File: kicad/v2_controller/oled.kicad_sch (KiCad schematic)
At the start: 9 parts, among them U2 SSD1306_I2C

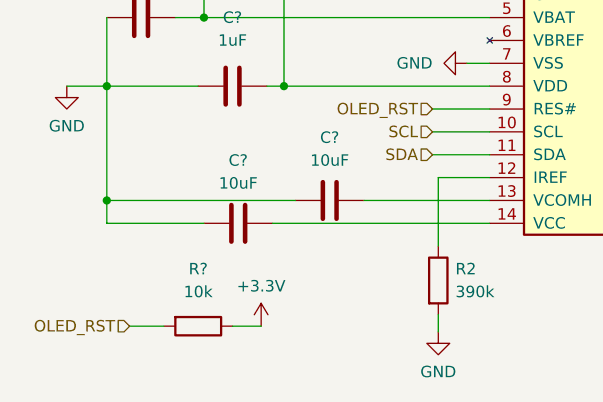
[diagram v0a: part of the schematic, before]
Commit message: [kicad] finish initial component placement
This will probably need to be tweaked further once I begin routing,
but is a start for now.
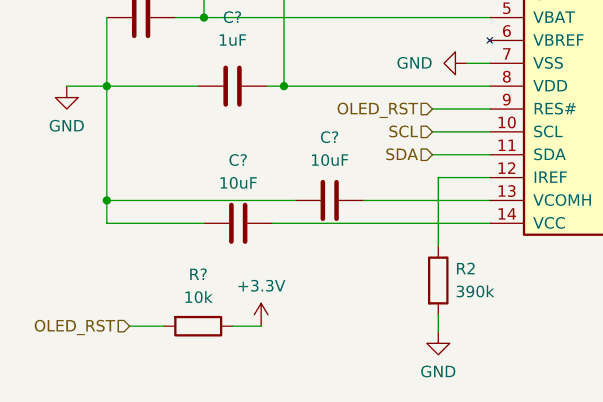
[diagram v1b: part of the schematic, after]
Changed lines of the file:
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@@
   (symbol (lib_id "Device:R") (at 52.705 85.725 270) (unit 1)
     (in_bom yes) (on_board yes) (dnp no) (fields_autoplaced)
-    (property "Reference" "R?" (at 52.705 79.375 90)
-      (effects (font (size 1.27 1.27)))
-    )
-    (property "Value" "10k" (at 52.705 81.915 90)
+    (property "Reference" "R?" (at 52.705 80.01 90)
+      (effects (font (size 1.27 1.27)))
+    )
+    (property "Value" "10k" (at 52.705 82.55 90)
       (effects (font (size 1.27 1.27)))
     )
@@
         )
         (path "/102c646f-89e8-474a-be69-05b634400329/e9d106a9-5000-4667-94d4-a7bfa9242bd9"
-          (reference "R2") (unit 1)
+          (reference "R17") (unit 1)
         )
       )
@@
         )
         (path "/102c646f-89e8-474a-be69-05b634400329/e9d106a9-5000-4667-94d4-a7bfa9242bd9"
-          (reference "R3") (unit 1)
-        )
-      )
+          (reference "R18") (unit 1)
+        )
+      )

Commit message: [kicad] switch OLED to mount on the back, folding the FPC connector
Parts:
- U2: footprint mantyl:SSD1306_OLED-0.91-128x32_Back_Mount -> mantyl:SSD1306_OLED-0.91-128x32_Folded
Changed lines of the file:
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@@
       (effects (font (size 1.27 1.27)) (justify left))
     )
-    (property "Footprint" "mantyl:SSD1306_OLED-0.91-128x32_Back_Mount" (at 90.17 56.515 0)
+    (property "Footprint" "mantyl:SSD1306_OLED-0.91-128x32_Folded" (at 90.17 56.515 0)
       (effects (font (size 1.27 1.27)) hide)
     )

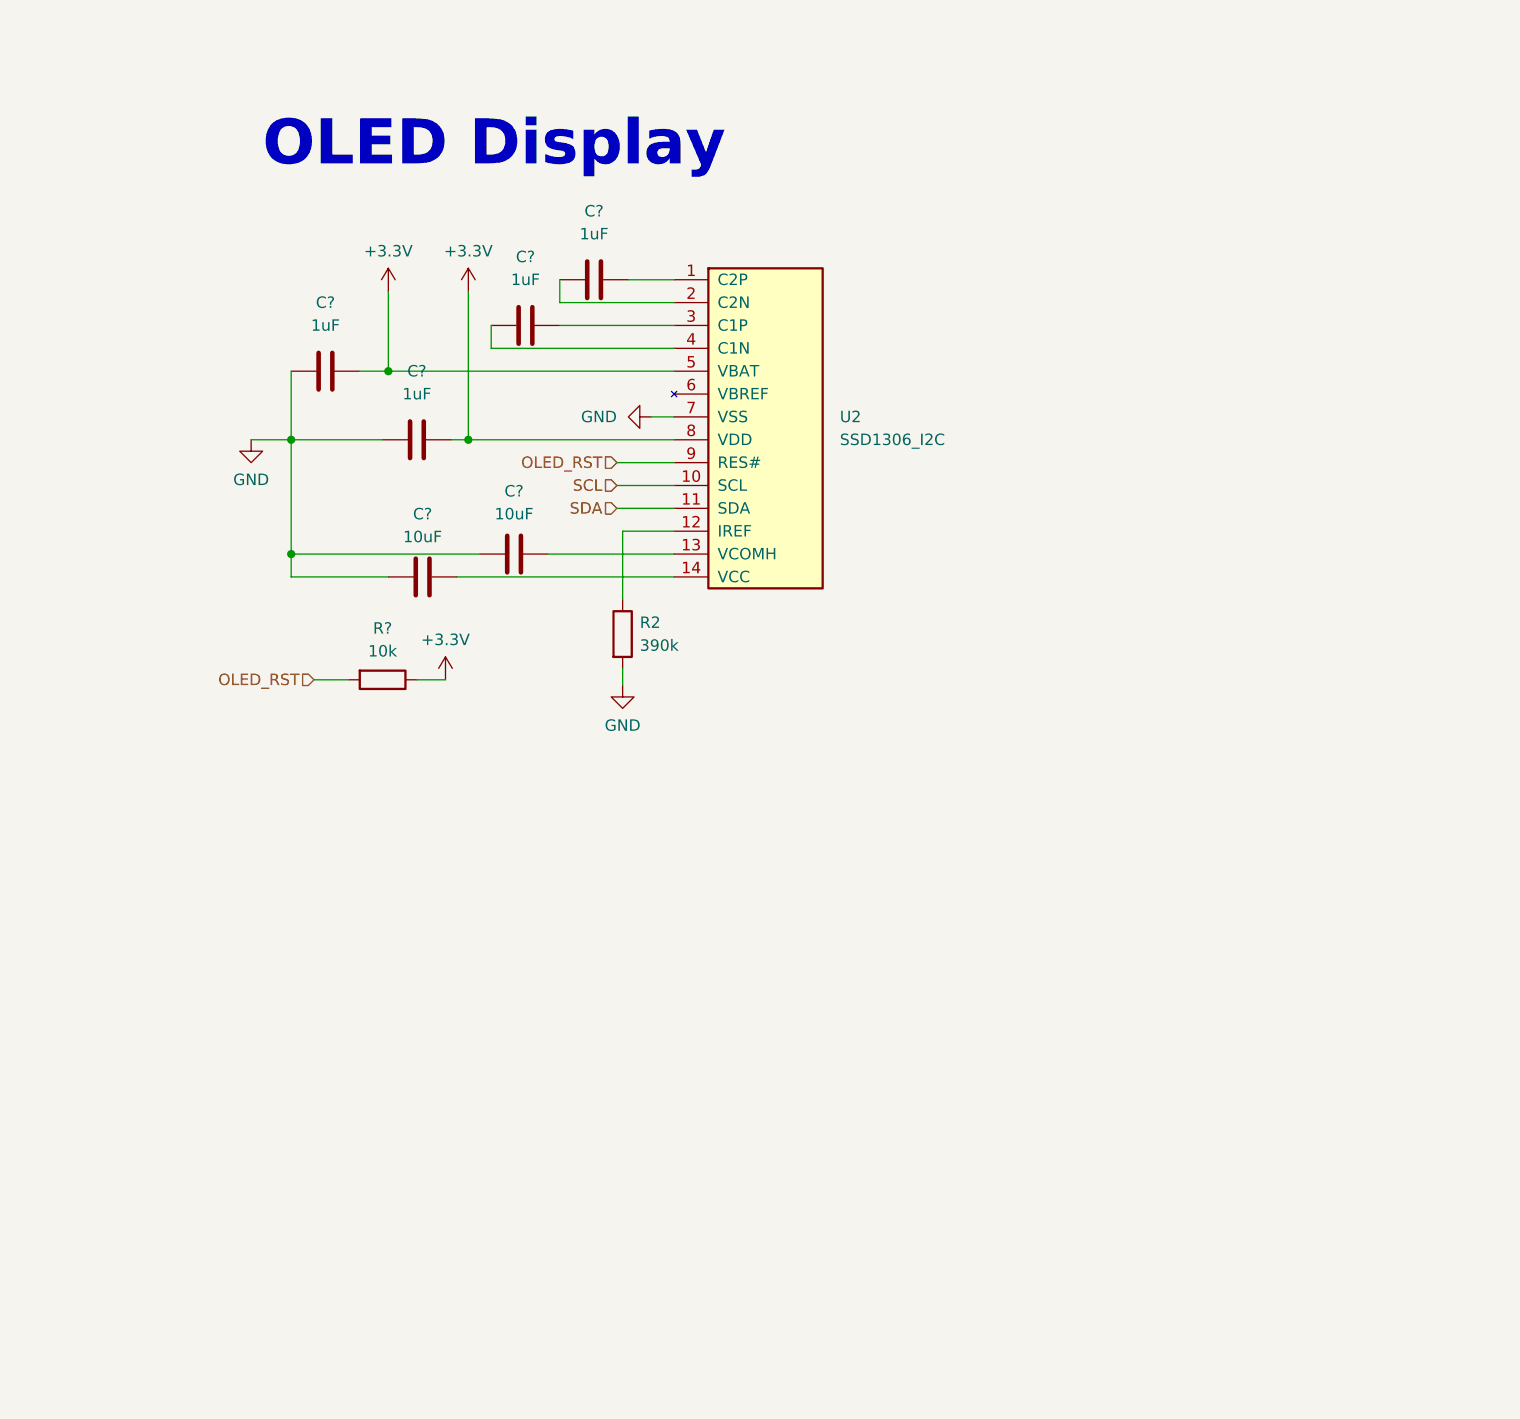
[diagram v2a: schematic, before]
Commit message: [kicad] connect mounting holes to ground
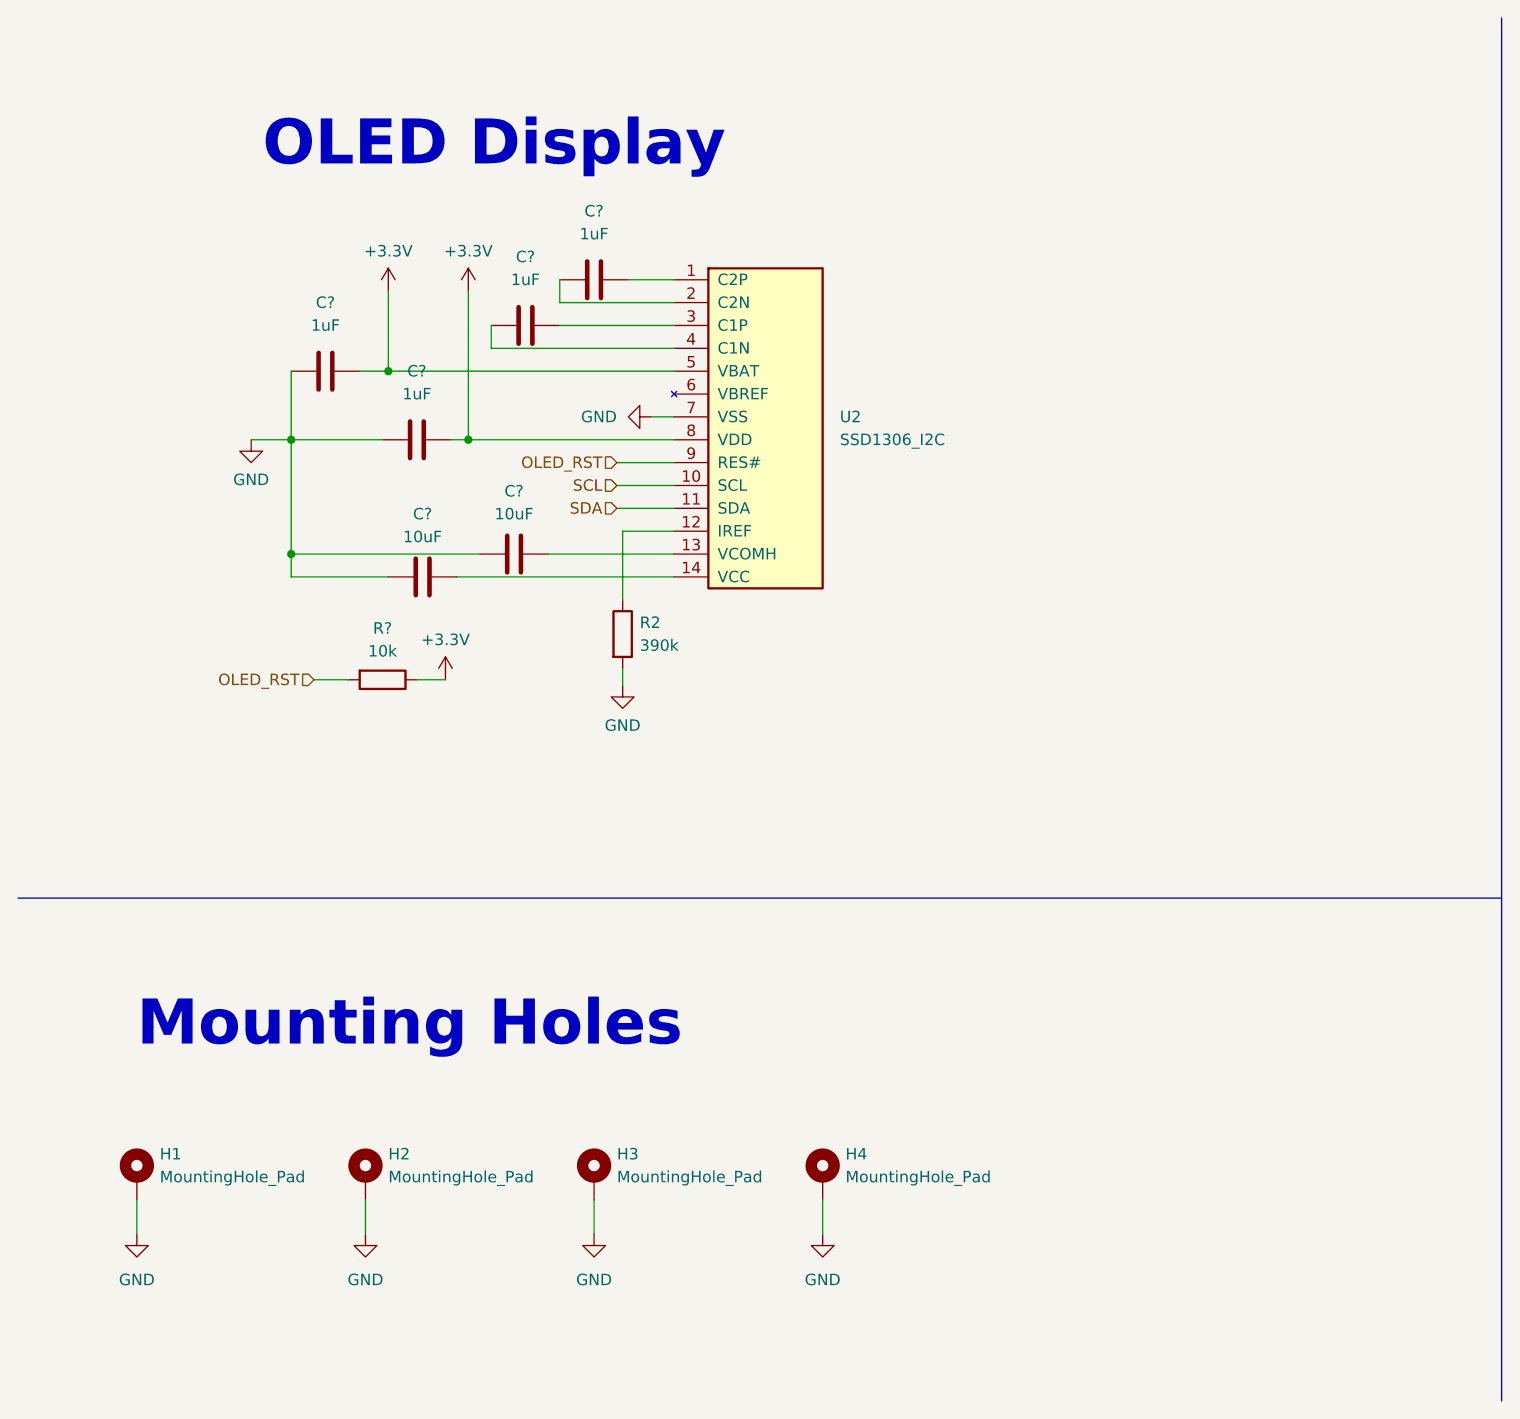
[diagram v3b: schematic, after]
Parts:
- added H1, H2, H3, H4: MountingHole_Pad, MountingHole:MountingHole_2.7mm_M2.5_Pad_Via, symbol Mechanical:MountingHole_Pad
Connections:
- net GND: now also H1.1, H2.1, H3.1, H4.1
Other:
- note added: "Mounting Holes"
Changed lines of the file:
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@@
+    (stroke (width 0) (type default))
+  )
+  (wire (pts (xy 25.4 143.51) (xy 25.4 147.32))
     (stroke (width 0) (type default))
   )
@@
     (stroke (width 0) (type default))
   )
+  (polyline (pts (xy 177.038 165.862) (xy 177.038 12.192))
+    (stroke (width 0) (type default))
+  )
   (wire (pts (xy 85.09 59.055) (xy 62.23 59.055))
     (stroke (width 0) (type default))
@@
     (stroke (width 0) (type default))
   )
+  (polyline (pts (xy 12.192 109.982) (xy 177.038 109.982))
+    (stroke (width 0) (type default))
+  )
   (wire (pts (xy 72.39 43.815) (xy 72.39 41.275))
     (stroke (width 0) (type default))
   )
+  (wire (pts (xy 76.2 143.51) (xy 76.2 147.32))
+    (stroke (width 0) (type default))
+  )
   (wire (pts (xy 42.545 71.755) (xy 42.545 59.055))
     (stroke (width 0) (type default))
@@
     (stroke (width 0) (type default))
   )
+  (wire (pts (xy 50.8 143.51) (xy 50.8 147.32))
+    (stroke (width 0) (type default))
+  )
+  (wire (pts (xy 101.6 143.51) (xy 101.6 147.32))
+    (stroke (width 0) (type default))
+  )
   (wire (pts (xy 42.545 74.295) (xy 42.545 71.755))
     (stroke (width 0) (type default))
@@
   (wire (pts (xy 50.165 51.435) (xy 53.34 51.435))
     (stroke (width 0) (type default))
+  )
+  (text "Mounting Holes" (at 25.4 127 0)
+    (effects (font (size 5 5) (thickness 1) bold (color 194 0 0 1)) (justify left bottom))
   )
   (text "OLED Display" (at 39.37 29.21 0)
@@
     )
   )
+  (symbol (lib_id "power:GND") (at 25.4 147.32 0) (unit 1)
+    (in_bom yes) (on_board yes) (dnp no) (fields_autoplaced)
+    (property "Reference" "#PWR021" (at 25.4 153.67 0)
+      (effects (font (size 1.27 1.27)) hide)
+    )
+    (property "Value" "GND" (at 25.4 152.4 0)
+      (effects (font (size 1.27 1.27)))
+    )
+    (property "Footprint" "" (at 25.4 147.32 0)
+      (effects (font (size 1.27 1.27)) hide)
+    )
+    (property "Datasheet" "" (at 25.4 147.32 0)
+      (effects (font (size 1.27 1.27)) hide)
+    )
+    (pin "1")
+    (instances
+      (project "v2_controller"
+        (path "/102c646f-89e8-474a-be69-05b634400329/e9d106a9-5000-4667-94d4-a7bfa9242bd9"
+          (reference "#PWR021") (unit 1)
+        )
+      )
+    )
+  )
   (symbol (lib_id "power:+3.3V") (at 59.69 85.725 0) (unit 1)
     (in_bom yes) (on_board yes) (dnp no) (fields_autoplaced)
@@
         (path "/102c646f-89e8-474a-be69-05b634400329/e9d106a9-5000-4667-94d4-a7bfa9242bd9"
           (reference "#PWR083") (unit 1)
+        )
+      )
+    )
+  )
+  (symbol (lib_id "power:GND") (at 76.2 147.32 0) (unit 1)
+    (in_bom yes) (on_board yes) (dnp no) (fields_autoplaced)
+    (property "Reference" "#PWR089" (at 76.2 153.67 0)
+      (effects (font (size 1.27 1.27)) hide)
+    )
+    (property "Value" "GND" (at 76.2 152.4 0)
+      (effects (font (size 1.27 1.27)))
+    )
+    (property "Footprint" "" (at 76.2 147.32 0)
+      (effects (font (size 1.27 1.27)) hide)
+    )
+    (property "Datasheet" "" (at 76.2 147.32 0)
+      (effects (font (size 1.27 1.27)) hide)
+    )
+    (pin "1")
+    (instances
+      (project "v2_controller"
+        (path "/102c646f-89e8-474a-be69-05b634400329/e9d106a9-5000-4667-94d4-a7bfa9242bd9"
+          (reference "#PWR089") (unit 1)
+        )
+      )
+    )
+  )
+  (symbol (lib_id "power:GND") (at 101.6 147.32 0) (unit 1)
+    (in_bom yes) (on_board yes) (dnp no) (fields_autoplaced)
+    (property "Reference" "#PWR090" (at 101.6 153.67 0)
+      (effects (font (size 1.27 1.27)) hide)
+    )
+    (property "Value" "GND" (at 101.6 152.4 0)
+      (effects (font (size 1.27 1.27)))
+    )
+    (property "Footprint" "" (at 101.6 147.32 0)
+      (effects (font (size 1.27 1.27)) hide)
+    )
+    (property "Datasheet" "" (at 101.6 147.32 0)
+      (effects (font (size 1.27 1.27)) hide)
+    )
+    (pin "1")
+    (instances
+      (project "v2_controller"
+        (path "/102c646f-89e8-474a-be69-05b634400329/e9d106a9-5000-4667-94d4-a7bfa9242bd9"
+          (reference "#PWR090") (unit 1)
         )
       )
@@
     )
   )
+  (symbol (lib_id "Mechanical:MountingHole_Pad") (at 101.6 140.97 0) (unit 1)
+    (in_bom no) (on_board yes) (dnp no) (fields_autoplaced)
+    (property "Reference" "H4" (at 104.14 138.43 0)
+      (effects (font (size 1.27 1.27)) (justify left))
+    )
+    (property "Value" "MountingHole_Pad" (at 104.14 140.97 0)
+      (effects (font (size 1.27 1.27)) (justify left))
+    )
+    (property "Footprint" "MountingHole:MountingHole_2.7mm_M2.5_Pad_Via" (at 101.6 140.97 0)
+      (effects (font (size 1.27 1.27)) hide)
+    )
+    (property "Datasheet" "~" (at 101.6 140.97 0)
+      (effects (font (size 1.27 1.27)) hide)
+    )
+    (property "LCSC Part #" "" (at 101.6 140.97 0)
+      (effects (font (size 1.27 1.27)) hide)
+    )
+    (property "Manufacturer Part #" "" (at 101.6 140.97 0)
+      (effects (font (size 1.27 1.27)) hide)
+    )
+    (pin "1")
+    (instances
+      (project "v2_controller"
+        (path "/102c646f-89e8-474a-be69-05b634400329/e9d106a9-5000-4667-94d4-a7bfa9242bd9"
+          (reference "H4") (unit 1)
+        )
+      )
+    )
+  )
   (symbol (lib_id "power:GND") (at 79.375 86.36 0) (unit 1)
     (in_bom yes) (on_board yes) (dnp no) (fields_autoplaced)
@@
         (path "/102c646f-89e8-474a-be69-05b634400329/e9d106a9-5000-4667-94d4-a7bfa9242bd9"
           (reference "#PWR075") (unit 1)
+        )
+      )
+    )
+  )
+  (symbol (lib_id "Mechanical:MountingHole_Pad") (at 50.8 140.97 0) (unit 1)
+    (in_bom no) (on_board yes) (dnp no) (fields_autoplaced)
+    (property "Reference" "H2" (at 53.34 138.43 0)
+      (effects (font (size 1.27 1.27)) (justify left))
+    )
+    (property "Value" "MountingHole_Pad" (at 53.34 140.97 0)
+      (effects (font (size 1.27 1.27)) (justify left))
+    )
+    (property "Footprint" "MountingHole:MountingHole_2.7mm_M2.5_Pad_Via" (at 50.8 140.97 0)
+      (effects (font (size 1.27 1.27)) hide)
+    )
+    (property "Datasheet" "~" (at 50.8 140.97 0)
+      (effects (font (size 1.27 1.27)) hide)
+    )
+    (property "LCSC Part #" "" (at 50.8 140.97 0)
+      (effects (font (size 1.27 1.27)) hide)
+    )
+    (property "Manufacturer Part #" "" (at 50.8 140.97 0)
+      (effects (font (size 1.27 1.27)) hide)
+    )
+    (pin "1")
+    (instances
+      (project "v2_controller"
+        (path "/102c646f-89e8-474a-be69-05b634400329/e9d106a9-5000-4667-94d4-a7bfa9242bd9"
+          (reference "H2") (unit 1)
         )
       )
@@
     )
   )
+  (symbol (lib_id "Mechanical:MountingHole_Pad") (at 76.2 140.97 0) (unit 1)
+    (in_bom no) (on_board yes) (dnp no) (fields_autoplaced)
+    (property "Reference" "H3" (at 78.74 138.43 0)
+      (effects (font (size 1.27 1.27)) (justify left))
+    )
+    (property "Value" "MountingHole_Pad" (at 78.74 140.97 0)
+      (effects (font (size 1.27 1.27)) (justify left))
+    )
+    (property "Footprint" "MountingHole:MountingHole_2.7mm_M2.5_Pad_Via" (at 76.2 140.97 0)
+      (effects (font (size 1.27 1.27)) hide)
+    )
+    (property "Datasheet" "~" (at 76.2 140.97 0)
+      (effects (font (size 1.27 1.27)) hide)
+    )
+    (property "LCSC Part #" "" (at 76.2 140.97 0)
+      (effects (font (size 1.27 1.27)) hide)
+    )
+    (property "Manufacturer Part #" "" (at 76.2 140.97 0)
+      (effects (font (size 1.27 1.27)) hide)
+    )
+    (pin "1")
+    (instances
+      (project "v2_controller"
+        (path "/102c646f-89e8-474a-be69-05b634400329/e9d106a9-5000-4667-94d4-a7bfa9242bd9"
+          (reference "H3") (unit 1)
+        )
+      )
+    )
+  )
   (symbol (lib_id "Device:C") (at 68.58 46.355 90) (unit 1)
     (in_bom yes) (on_board yes) (dnp no) (fields_autoplaced)
@@
     )
   )
+  (symbol (lib_id "Mechanical:MountingHole_Pad") (at 25.4 140.97 0) (unit 1)
+    (in_bom no) (on_board yes) (dnp no) (fields_autoplaced)
+    (property "Reference" "H1" (at 27.94 138.43 0)
+      (effects (font (size 1.27 1.27)) (justify left))
+    )
+    (property "Value" "MountingHole_Pad" (at 27.94 140.97 0)
+      (effects (font (size 1.27 1.27)) (justify left))
+    )
+    (property "Footprint" "MountingHole:MountingHole_2.7mm_M2.5_Pad_Via" (at 25.4 140.97 0)
+      (effects (font (size 1.27 1.27)) hide)
+    )
+    (property "Datasheet" "~" (at 25.4 140.97 0)
+      (effects (font (size 1.27 1.27)) hide)
+    )
+    (property "LCSC Part #" "" (at 25.4 140.97 0)
+      (effects (font (size 1.27 1.27)) hide)
+    )
+    (property "Manufacturer Part #" "" (at 25.4 140.97 0)
+      (effects (font (size 1.27 1.27)) hide)
+    )
+    (pin "1")
+    (instances
+      (project "v2_controller"
+        (path "/102c646f-89e8-474a-be69-05b634400329/e9d106a9-5000-4667-94d4-a7bfa9242bd9"
+          (reference "H1") (unit 1)
+        )
+      )
+    )
+  )
   (symbol (lib_id "Device:R") (at 79.375 80.645 0) (unit 1)
     (in_bom yes) (on_board yes) (dnp no) (fields_autoplaced)
@@
         )
       )
+    )
+  )
+  (symbol (lib_id "power:GND") (at 50.8 147.32 0) (unit 1)
+    (in_bom yes) (on_board yes) (dnp no) (fields_autoplaced)
+    (property "Reference" "#PWR078" (at 50.8 153.67 0)
+      (effects (font (size 1.27 1.27)) hide)
+    )
+    (property "Value" "GND" (at 50.8 152.4 0)
+      (effects (font (size 1.27 1.27)))
+    )
+    (property "Footprint" "" (at 50.8 147.32 0)
+      (effects (font (size 1.27 1.27)) hide)
+    )
+    (property "Datasheet" "" (at 50.8 147.32 0)
+      (effects (font (size 1.27 1.27)) hide)
+    )
+    (pin "1")
+    (instances
+      (project "v2_controller"
+        (path "/102c646f-89e8-474a-be69-05b634400329/e9d106a9-5000-4667-94d4-a7bfa9242bd9"
+          (reference "#PWR078") (unit 1)
+        )
+      )
